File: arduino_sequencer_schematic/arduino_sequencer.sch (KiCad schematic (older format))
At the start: 174 parts, among them J1 AudioJack, J10 AudioJack, J11 AudioJack, J12 AudioJack, J13 AudioJack, J14 AudioJack, J15 AudioJack, J16 Conn_02x05, J2 AudioJack, J3 AudioJack, J4 AudioJack, J5 AudioJack, J6 AudioJack, J7 AudioJack, J8 AudioJack, J9 AudioJack, Q1 2N3904, Q10 2N3904, Q11 2N3904, Q2 2N3904, Q3 2N3904, Q4 2N3904, Q5 2N3904, Q6 2N3904, Q7 2N3904, Q8 2N3904, Q9 2N3904, SW1 SW_SPST, SW2 SW_Push, SW3 SW_Push, SW4 SW_Push, SW5 SW_SPST, SW6 SW_SPST, U1 74HC595, U2 TL084, U3 TL084, U4 L7805

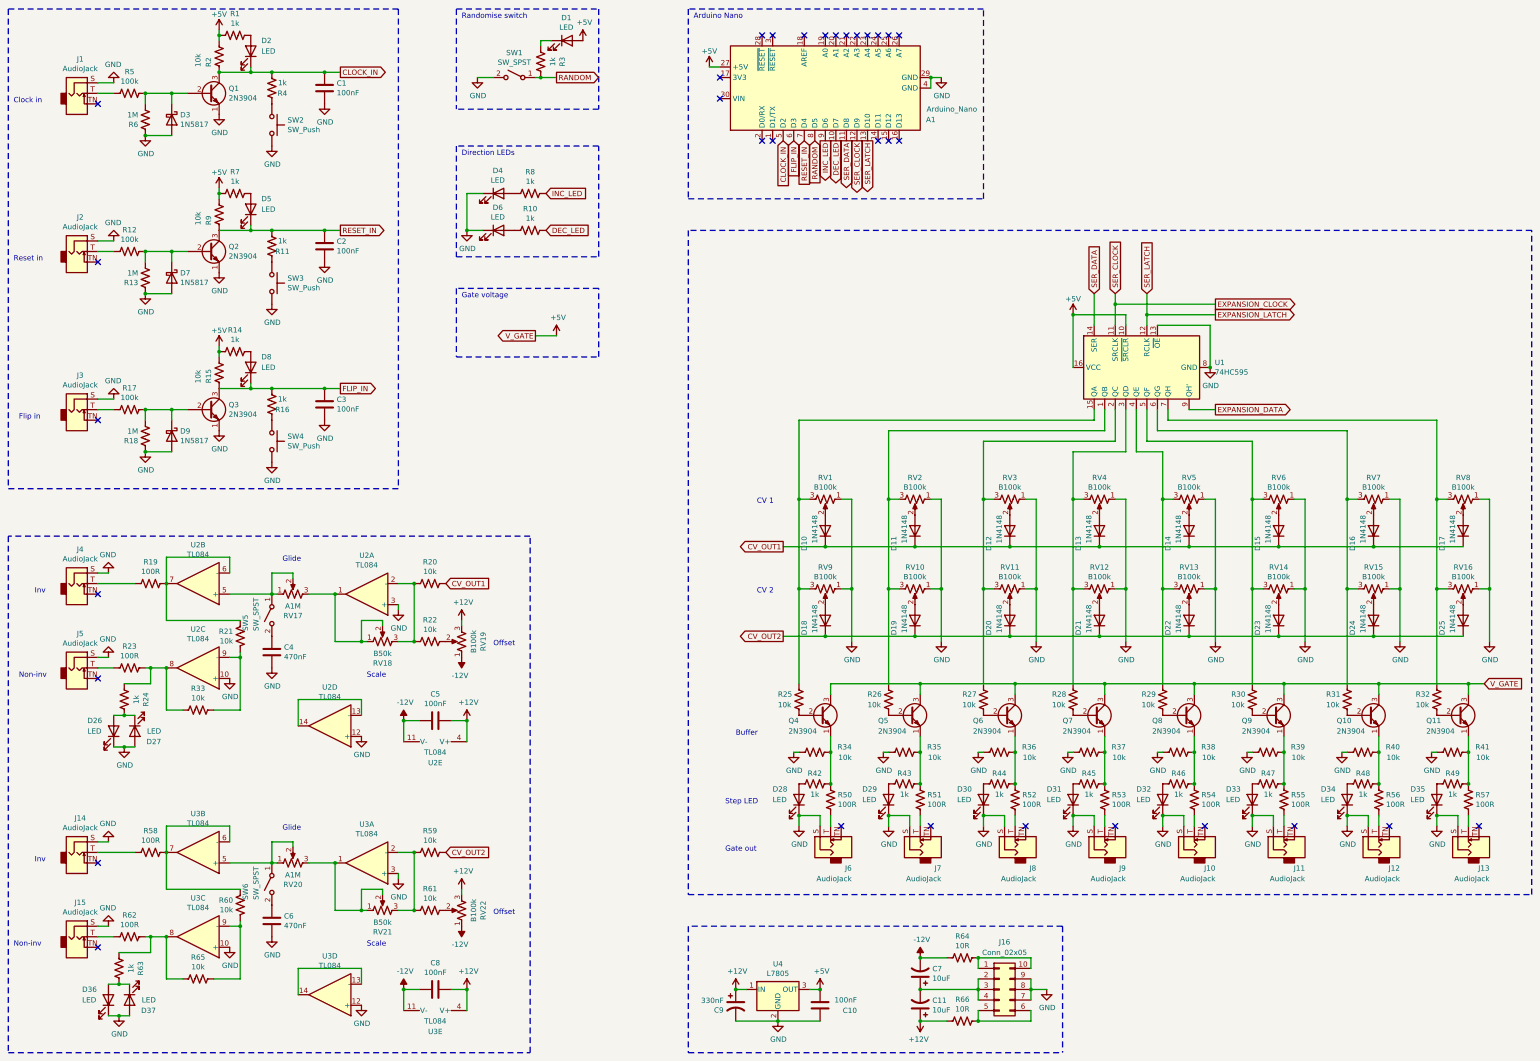
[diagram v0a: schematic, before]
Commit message: Changed gate voltage to 9V by default
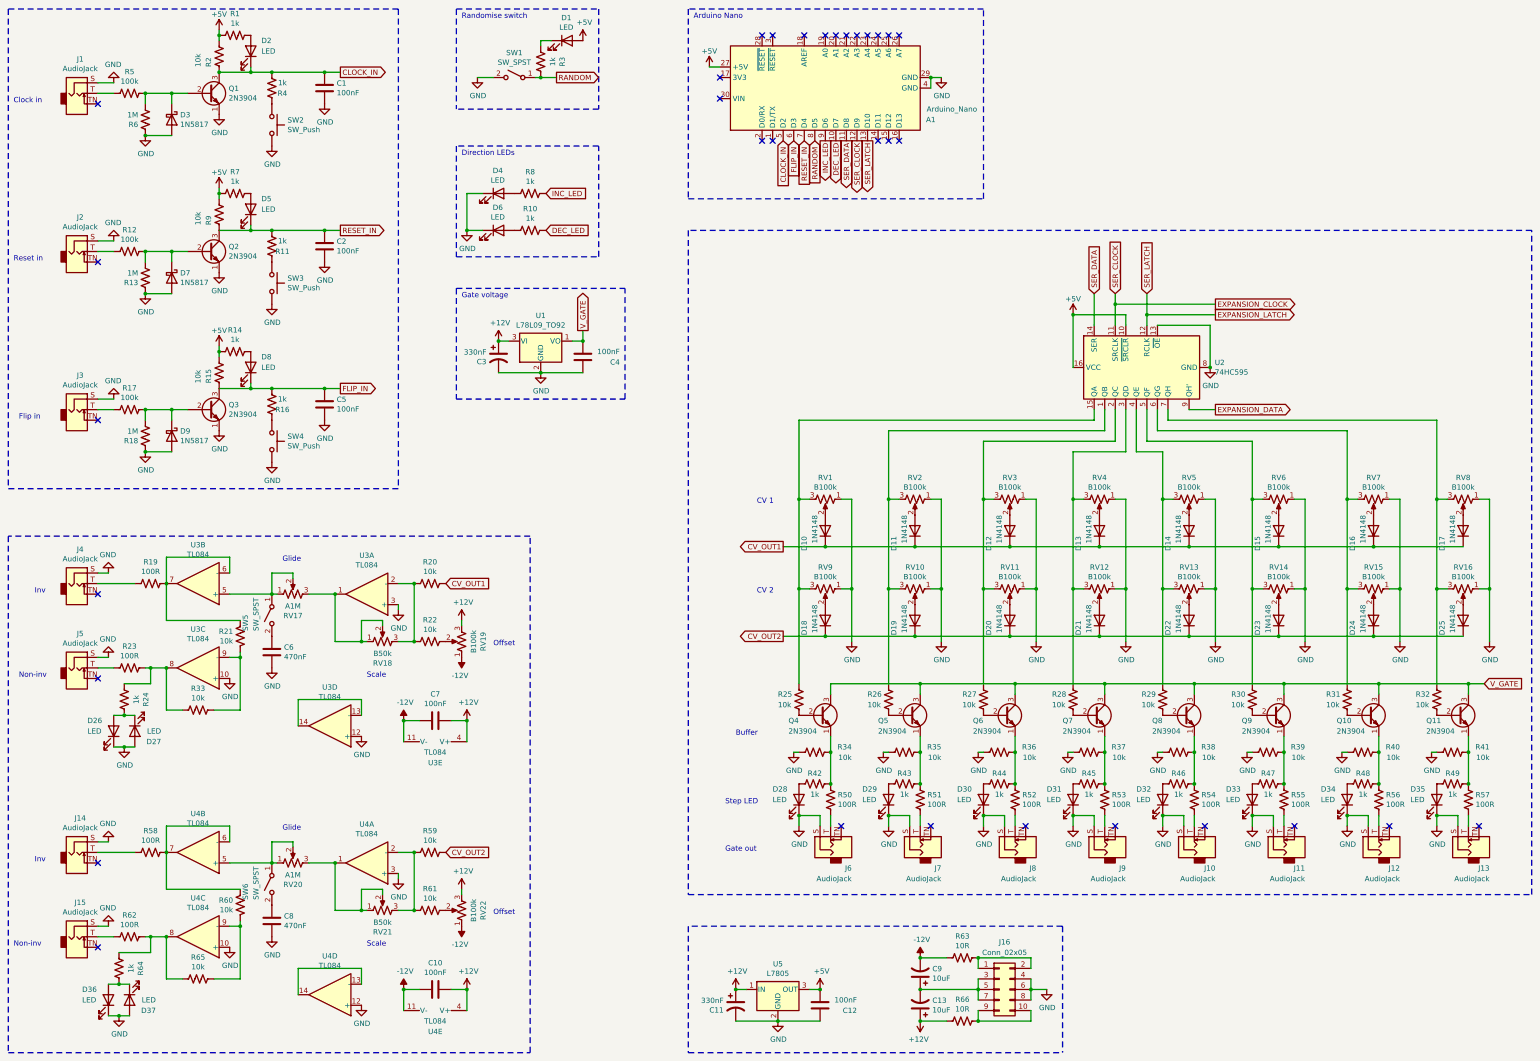
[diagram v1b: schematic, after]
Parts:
- removed J16: Conn_02x05, Connector_IDC:IDC-Header_2x05_P2.54mm_Vertical, symbol Connector_Generic:Conn_02x05_Counter_Clockwise
- added C3: 330nF, Capacitor_THT:CP_Radial_D10.0mm_P3.80mm, symbol Device:CP1
- added C4: 100nF, Capacitor_THT:C_Disc_D6.0mm_W2.5mm_P5.00mm, symbol Device:C
- added J16: Conn_02x05, Connector_IDC:IDC-Header_2x05_P2.54mm_Vertical, symbol Connector_Generic:Conn_02x05_Odd_Even
- added U1: L78L09_TO92, Package_TO_SOT_THT:TO-92_Inline, symbol Regulator_Linear:L78L09_TO92
- renumbered C8 to C10, C9 to C11, C10 to C12, C11 to C13, C3 to C5, C4 to C6, C5 to C7, C6 to C8, C7 to C9, R64 to R63, R63 to R64, U1 to U2, U2 to U3, U3 to U4, U4 to U5
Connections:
- net +12V: now also C3.1, U1.3 (VI)
- net +5V: no longer Q10.3 (C), Q11.3 (C), Q4.3 (C), Q5.3 (C), Q6.3 (C), Q7.3 (C), Q8.3 (C), Q9.3 (C)
- net GND: now also C3.2, C4.1, J16.4 (Pin_4), J16.6 (Pin_6), J16.8 (Pin_8), U1.2 (GND)
- net at R63.1: now also J16.1 (Pin_1), J16.2 (Pin_2)
- net at C13.2, C9.1: now also J16.3 (Pin_3), J16.5 (Pin_5), J16.7 (Pin_7)
- net at R66.1: now also J16.10 (Pin_10), J16.9 (Pin_9)
- new net V_GATE: C4.2, Q10.3 (C), Q11.3 (C), Q4.3 (C), Q5.3 (C), Q6.3 (C), Q7.3 (C), Q8.3 (C), Q9.3 (C), U1.1 (VO)

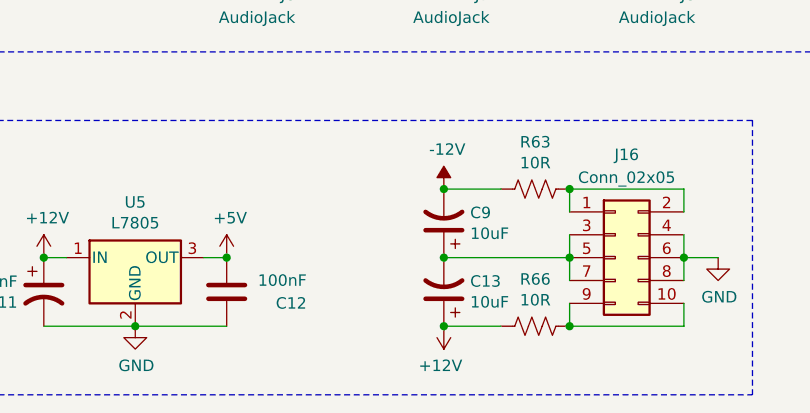
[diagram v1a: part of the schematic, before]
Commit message: added missing GND label
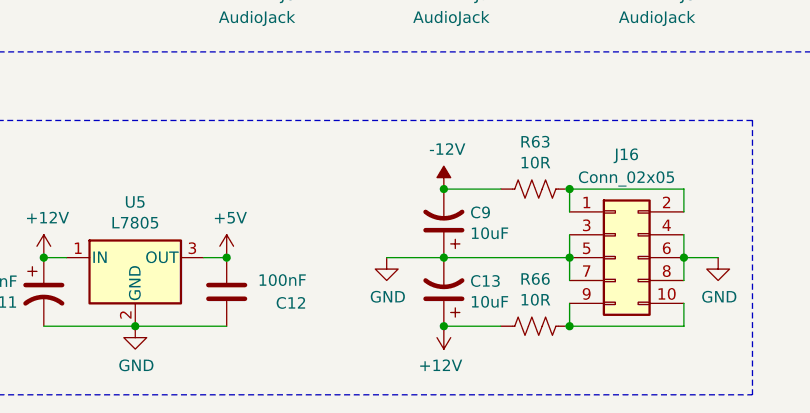
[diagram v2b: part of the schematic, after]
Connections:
- net GND: now also C13.2, C9.1, J16.3 (Pin_3), J16.5 (Pin_5), J16.7 (Pin_7)
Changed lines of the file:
@@
 Wire Notes Line
 	4900 3400 6500 3400
+$Comp
+L power:GND #PWR?
+U 1 1 5FEF4671
+P 9050 10050
+F 0 "#PWR?" H 9050 9800 50  0001 C CNN
+F 1 "GND" H 9055 9877 50  0000 C CNN
+F 2 "" H 9050 10050 50  0001 C CNN
+F 3 "" H 9050 10050 50  0001 C CNN
+	1    9050 10050
+	1    0    0    -1
+$EndComp
+Wire Wire Line
+	9050 10050 9300 10050
 $EndSCHEMATC

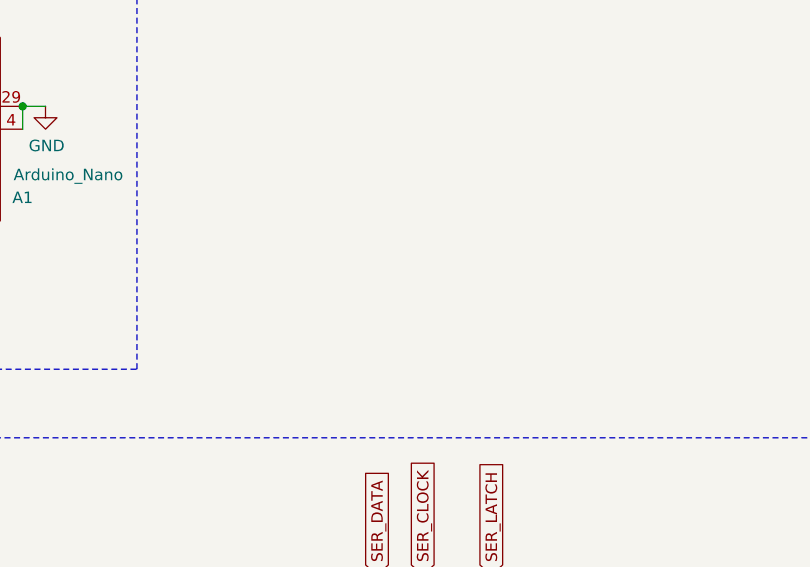
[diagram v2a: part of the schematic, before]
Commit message: Added expansion header
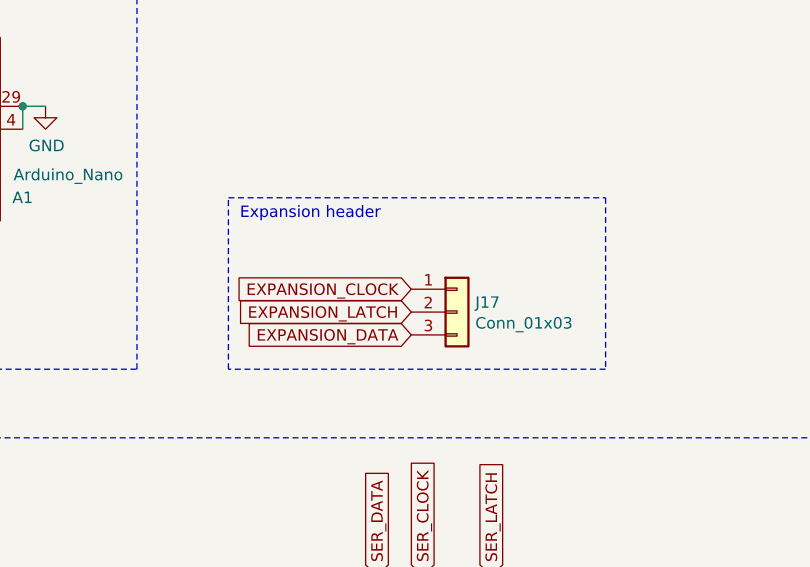
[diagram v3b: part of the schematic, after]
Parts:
- added J17: Conn_01x03, Connector_JST:JST_EH_B3B-EH-A_1x03_P2.50mm_Vertical, symbol Connector_Generic:Conn_01x03
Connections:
- net EXPANSION_CLOCK: now also J17.1 (Pin_1)
- net EXPANSION_DATA: now also J17.3 (Pin_3)
- net EXPANSION_LATCH: now also J17.2 (Pin_2)
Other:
- note added: "Expansion header"
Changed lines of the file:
@@
 	4900 3400 6500 3400
 $Comp
-L power:GND #PWR?
+L power:GND #PWR0101
 U 1 1 5FEF4671
 P 9050 10050
-F 0 "#PWR?" H 9050 9800 50  0001 C CNN
+F 0 "#PWR0101" H 9050 9800 50  0001 C CNN
 F 1 "GND" H 9055 9877 50  0000 C CNN
 F 2 "" H 9050 10050 50  0001 C CNN
@@
 Wire Wire Line
 	9050 10050 9300 10050
+$Comp
+L Connector_Generic:Conn_01x03 J17
+U 1 1 6007DC7F
+P 11300 2300
+F 0 "J17" H 11380 2342 50  0000 L CNN
+F 1 "Conn_01x03" H 11380 2251 50  0000 L CNN
+F 2 "Connector_JST:JST_EH_B3B-EH-A_1x03_P2.50mm_Vertical" H 11300 2300 50  0001 C CNN
+F 3 "~" H 11300 2300 50  0001 C CNN
+	1    11300 2300
+	1    0    0    -1
+$EndComp
+Text GLabel 11100 2300 0    50   Input ~ 0
+EXPANSION_LATCH
+Text GLabel 11100 2400 0    50   Input ~ 0
+EXPANSION_DATA
+Text GLabel 11100 2200 0    50   Input ~ 0
+EXPANSION_CLOCK
+Wire Notes Line
+	10300 2550 10300 1800
+Wire Notes Line
+	10300 1800 11950 1800
+Wire Notes Line
+	11950 1800 11950 2550
+Wire Notes Line
+	11950 2550 10300 2550
+Text Notes 10350 1900 0    50   ~ 0
+Expansion header
 $EndSCHEMATC

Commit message: Added resistor values on silkscreen
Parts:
- A1: footprint Module:Arduino_Nano -> TimMJN:Arduino_Nano_2x_header
- R1, R10, R11, R12, R13, R14, R15, R16, R17, R18, R19, R2, R20, R21, R22, R23, R24, R25, R26, R27, R28, R29, R3, R30, R31, R32, R33, R34, R35, R36, R37, R38, R39, R4, R40, R41, R42, R43, R44, R45, R46, R47, R48, R49, R5, R50, R51, R52, R53, R54, R55, R56, R57, R58, R59, R6, R60, R61, R62, R63, R64, R65, R66, R7, R8, R9: footprint Resistor_THT:R_Axial_DIN0207_L6.3mm_D2.5mm_P10.16mm_Horizontal -> TimMJN:R_Axial_DIN0207_L6.3mm_D2.5mm_P10.16mm_Horizontal_Value_SilkS
- SW2, SW3, SW4: footprint TimMJN:Mom_push_button -> TimMJN:Mom_push_button_PBS-110

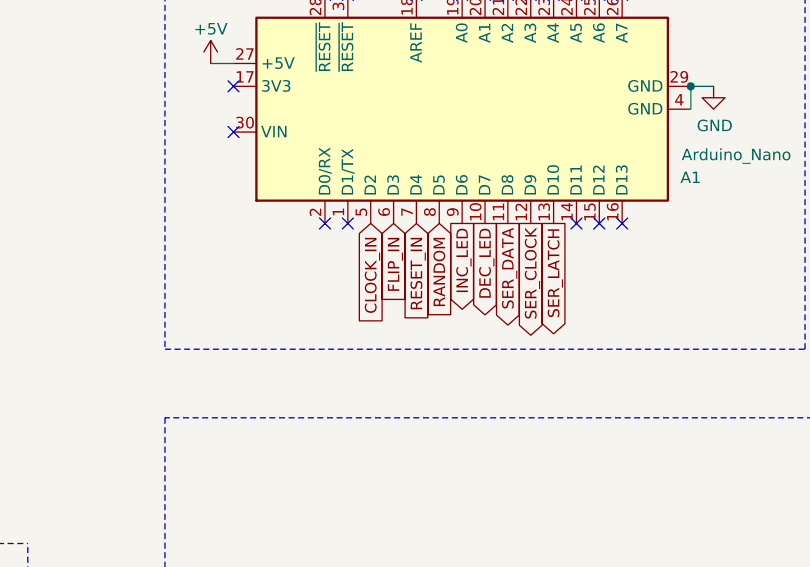
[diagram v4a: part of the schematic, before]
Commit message: fixed arduino reset/flip pin inconsistency
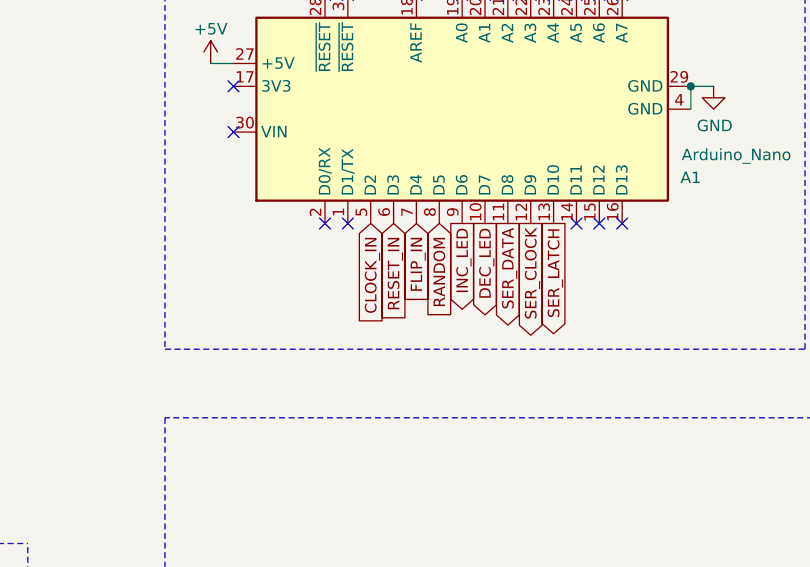
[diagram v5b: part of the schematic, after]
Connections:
- net FLIP_IN: now also A1.7 (D4); no longer A1.6 (D3)
- net RESET_IN: now also A1.6 (D3); no longer A1.7 (D4)
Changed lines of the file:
@@
 Text GLabel 8000 2000 3    50   Input ~ 0
 CLOCK_IN
+Text GLabel 8200 2000 3    50   Input ~ 0
+FLIP_IN
 Text GLabel 8100 2000 3    50   Input ~ 0
-FLIP_IN
-Text GLabel 8200 2000 3    50   Input ~ 0
 RESET_IN
 $Comp
